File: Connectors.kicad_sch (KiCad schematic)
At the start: 16 parts, among them U2 LT3042IMSE

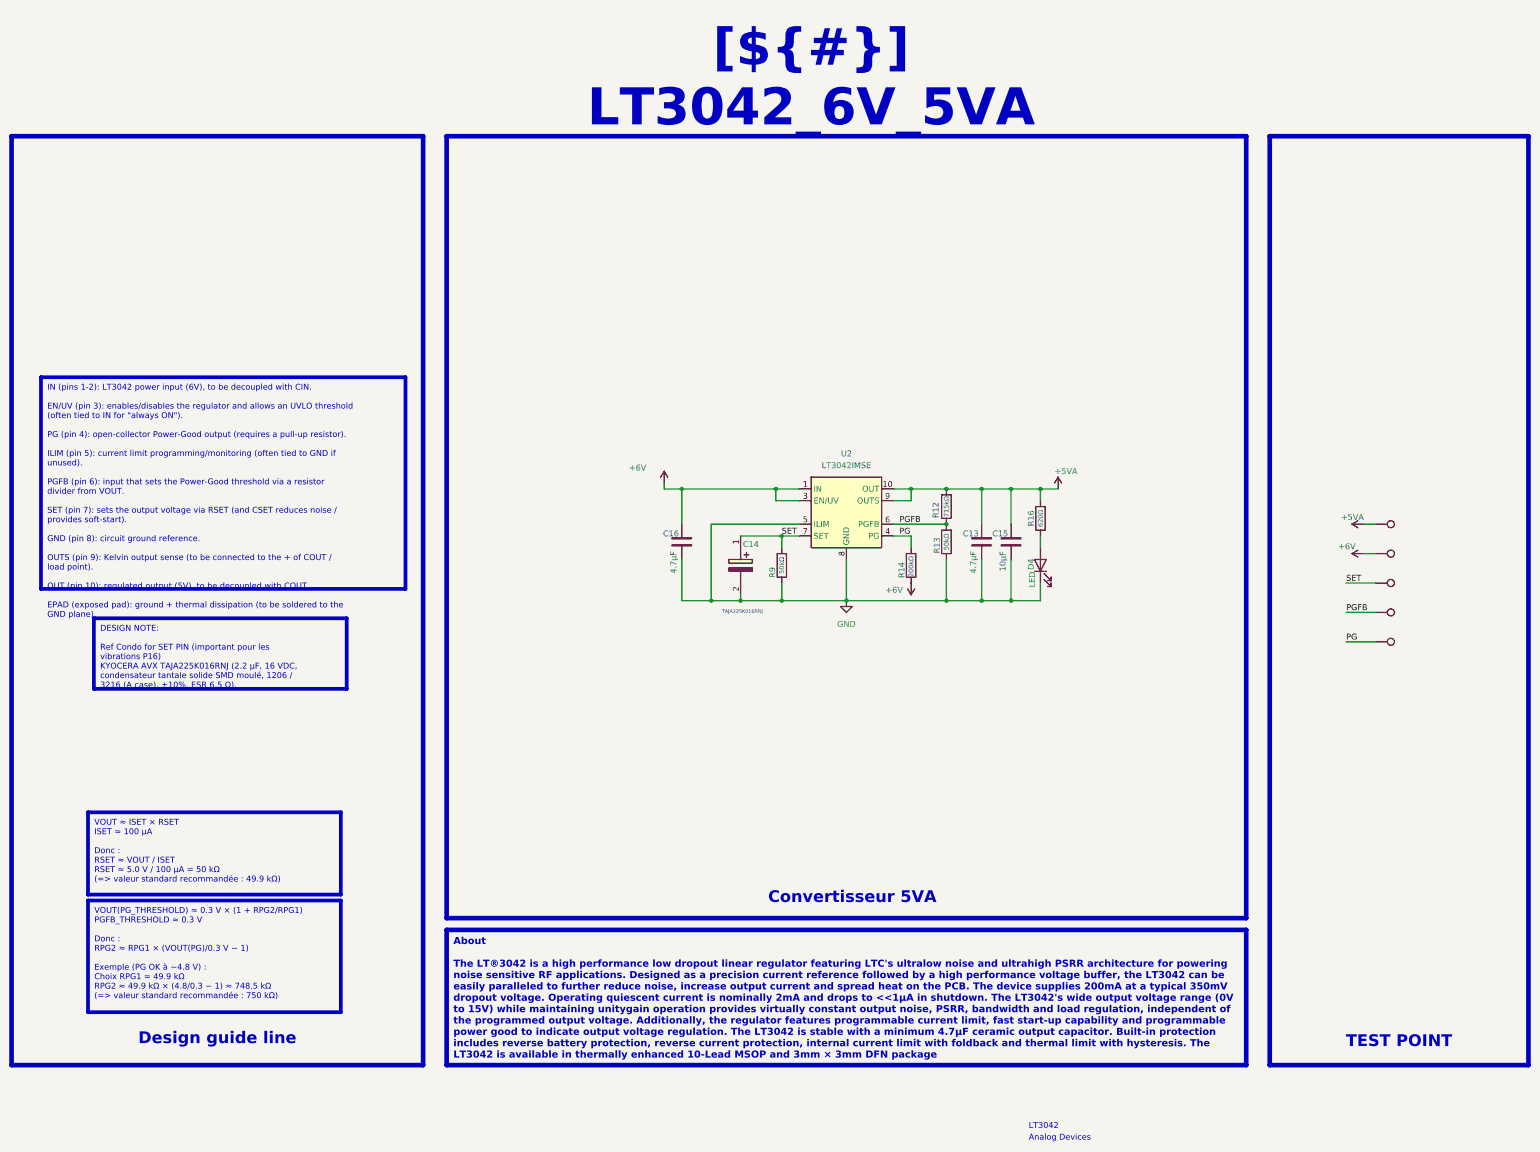
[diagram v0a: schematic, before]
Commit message: Clean up project for KDT template: rename, metadata, KiCad 10 CI
- Rename project Cellule_de_force_V2 -> OPEN_WEIGHT and sheets after their function
  (fix AD7910 -> AD7190 typo), update all sheet/project references in sch/pcb/pro
- Real title-block titles, sheet headers use ${TITLE}, restore KDT drawing sheets,
  remove template leftovers from PCB title block
- kibot_main.yaml: COMPANY = OPEN THRUST LAB, GIT_URL = foukouda/OPEN_WEIGHT
- CI: add KiCad 10 (KiBot v2_dk10), PRELIMINARY variant on dev
- README now generated from kibot_resources/templates/readme.txt; fill CHANGELOG
- Move mechanical CAD to Mechanical/, extend .gitignore, untrack 3Dx logs

Co-Authored-By: Claude Opus 5.5 <noreply@anthropic.com>
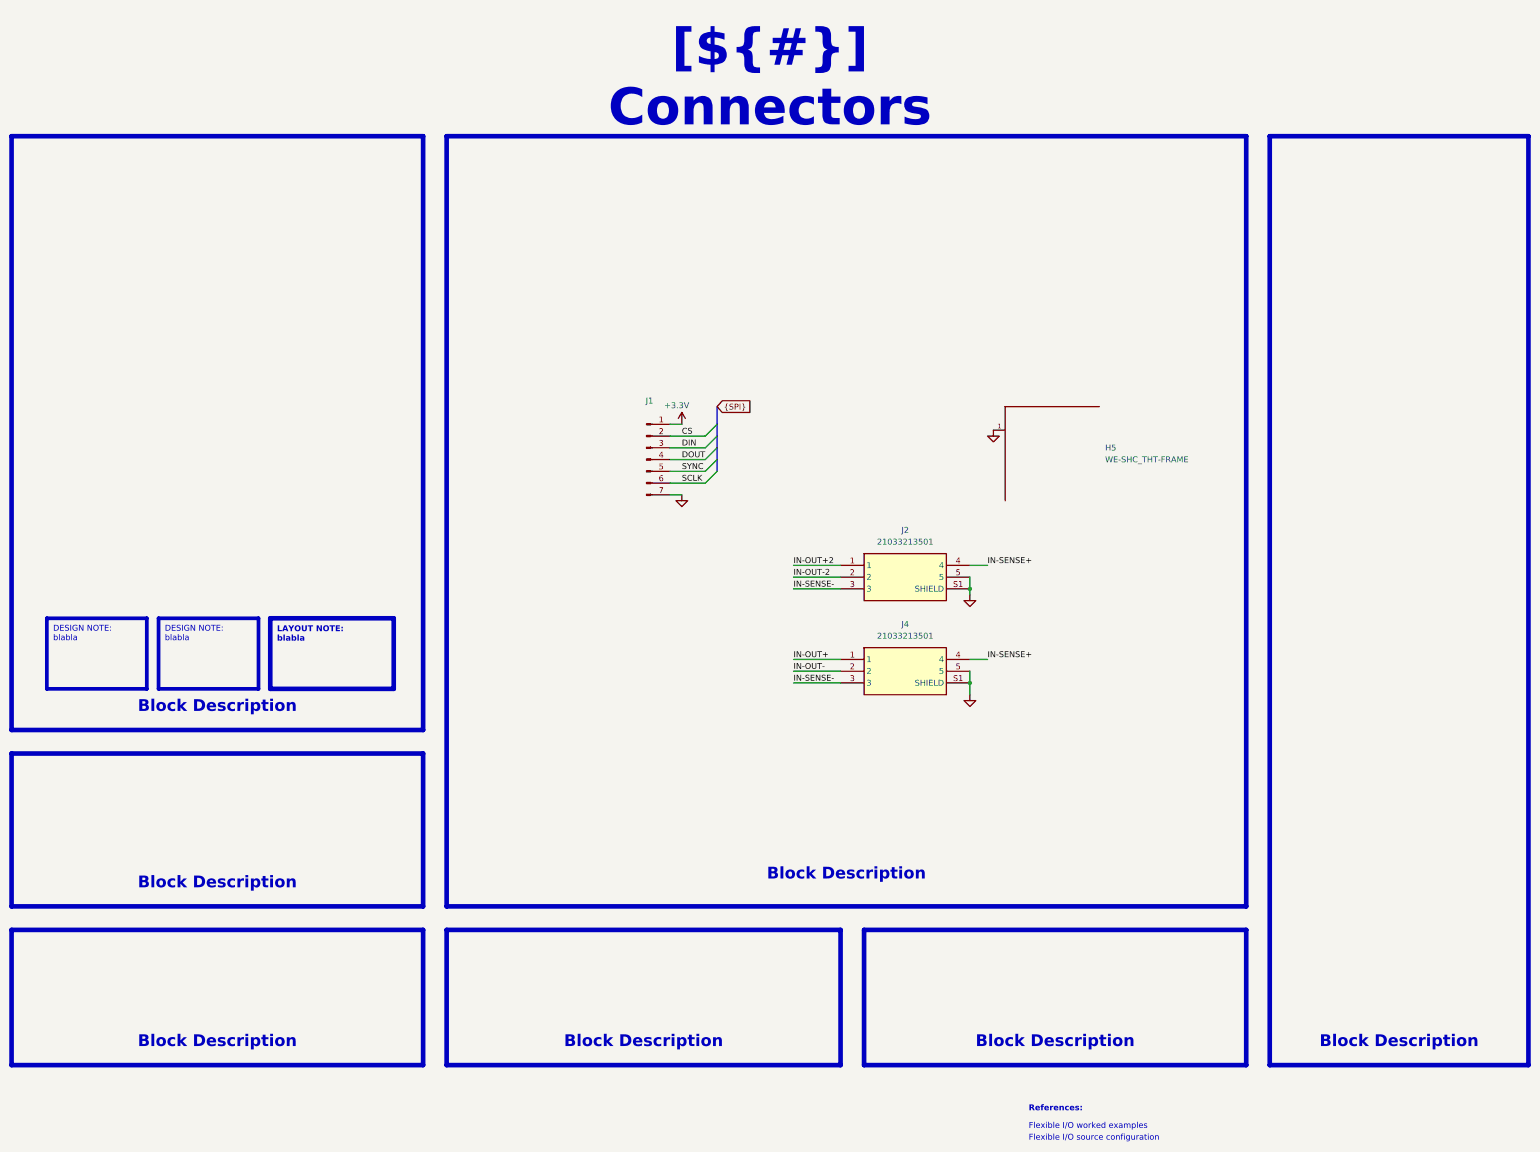
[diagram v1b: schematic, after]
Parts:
- removed C13, C16: 4.7µF, Capacitor_SMD:C_0603_1608Metric, symbol Device:C
- removed C14: TAJA225K016RNJ, CAPPM3216X180N, symbol TAJA225K016RNJ:TAJA225K016RNJ
- removed C15: 10µF, Capacitor_SMD:C_0603_1608Metric, symbol Device:C
- removed D4: LED, LED_SMD:LED_0603_1608Metric, symbol Device:LED
- removed R12: 715kΩ, Resistor_SMD:R_0603_1608Metric, symbol Device:R
- removed R13, R9: 50kΩ, Resistor_SMD:R_0603_1608Metric, symbol Device:R
- removed R14: 200kΩ, Resistor_SMD:R_0603_1608Metric, symbol Device:R
- removed R16: 620Ω, Resistor_SMD:R_0603_1608Metric, symbol Device:R
- removed TP10, TP11, TP12, TP13, TP17: TestPoint, TestPoint:TestPoint_Pad_D1.5mm, symbol Connector:TestPoint
- removed U2: LT3042IMSE, Package_SO:MSOP-10-1EP_3x3mm_P0.5mm_EP2.2x3.1mm_Mask1.83x1.89mm_ThermalVias, symbol Regulator_Linear:LT3042xMSE
- added H5: WE-SHC_THT-FRAME, WE-SHC_THT-FRAME:WE-SHC_THT-FRAME_36503205, symbol WE-SHC_THT-FRAME:WE-SHC_THT-FRAME
- added J1: Conn_01x07_Pin, Connector_JST:JST_XH_B7B-XH-AM_1x07_P2.50mm_Vertical, symbol Connector:Conn_01x07_Pin
- added J2, J4: 21033213501, 21033213501, symbol 21033213501:21033213501
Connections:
- net GND: now also H5.1, H5.10, H5.11, H5.12, H5.13, H5.14, H5.15, H5.16, H5.17, H5.2, H5.3, H5.4, H5.5, H5.6, H5.7, H5.9, J1.7 (Pin_7), J2.5, J2.S1 (SHIELD), J4.5, J4.S1 (SHIELD)
- new net +3.3V: J1.1 (Pin_1)
- new net CS: J1.2 (Pin_2)
- new net DIN: J1.3 (Pin_3)
- new net DOUT: J1.4 (Pin_4)
- new net IN-OUT+: J4.1
- new net IN-OUT+2: J2.1
- new net IN-OUT-: J4.2
- new net IN-OUT-2: J2.2
- new net IN-SENSE+: J2.4, J4.4
- new net IN-SENSE-: J2.3, J4.3
- new net SCLK: J1.6 (Pin_6)
- new net SYNC: J1.5 (Pin_5)
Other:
- note added: "Flexible I/O source configuration"
- note added: "Flexible I/O worked examples"
- note added: "References:"
- note removed: "Analog Devices"
- note removed: "LT3042"
- title: Sheet Title B -> Connectors

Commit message: Fix load-cell connectivity between Connectors and AD7190 sheets
IN-OUT/IN-SENSE were local labels on two sheets, so the connectors were not
connected to the ADC in the schematic. Convert them to global labels (IN-SENSE
merged into SENSE), and align label polarity on J2/J4 with the routed copper.

Co-Authored-By: Claude Opus 5.5 <noreply@anthropic.com>
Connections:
- net IN-SENSE+ renamed SENSE-
- net IN-SENSE- renamed SENSE+
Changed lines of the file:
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@@
 		)
 	)
-	(label "IN-SENSE+"
+	(global_label "SENSE-"
+		(shape bidirectional)
 		(at 256.54 152.4 0)
-		(effects
-			(font
-				(size 1.27 1.27)
-			)
-			(justify left bottom)
+		(fields_autoplaced yes)
+		(effects
+			(font
+				(size 1.27 1.27)
+			)
+			(justify left)
+		)
+		(property "Intersheetrefs" "${INTERSHEET_REFS}"
+			(at 266.5400 152.4 0)
+			(hide yes)
+			(show_name no)
+			(do_not_autoplace no)
+			(effects
+				(font
+					(size 1.27 1.27)
+				)
+				(justify left)
+			)
 		)
 	)
@@
 		)
 	)
-	(label "IN-SENSE+"
+	(global_label "SENSE-"
+		(shape bidirectional)
 		(at 256.54 132.08 0)
-		(effects
-			(font
-				(size 1.27 1.27)
-			)
-			(justify left bottom)
-		)
-	)
-	(label "IN-SENSE-"
+		(fields_autoplaced yes)
+		(effects
+			(font
+				(size 1.27 1.27)
+			)
+			(justify left)
+		)
+		(property "Intersheetrefs" "${INTERSHEET_REFS}"
+			(at 266.5400 132.08 0)
+			(hide yes)
+			(show_name no)
+			(do_not_autoplace no)
+			(effects
+				(font
+					(size 1.27 1.27)
+				)
+				(justify left)
+			)
+		)
+	)
+	(global_label "SENSE+"
+		(shape bidirectional)
 		(at 214.63 137.16 0)
-		(effects
-			(font
-				(size 1.27 1.27)
-			)
-			(justify left bottom)
+		(fields_autoplaced yes)
+		(effects
+			(font
+				(size 1.27 1.27)
+			)
+			(justify left)
+		)
+		(property "Intersheetrefs" "${INTERSHEET_REFS}"
+			(at 224.6300 137.16 0)
+			(hide yes)
+			(show_name no)
+			(do_not_autoplace no)
+			(effects
+				(font
+					(size 1.27 1.27)
+				)
+				(justify left)
+			)
 		)
 	)
@@
 		)
 	)
-	(label "IN-SENSE-"
+	(global_label "SENSE+"
+		(shape bidirectional)
 		(at 214.63 157.48 0)
-		(effects
-			(font
-				(size 1.27 1.27)
-			)
-			(justify left bottom)
+		(fields_autoplaced yes)
+		(effects
+			(font
+				(size 1.27 1.27)
+			)
+			(justify left)
+		)
+		(property "Intersheetrefs" "${INTERSHEET_REFS}"
+			(at 224.6300 157.48 0)
+			(hide yes)
+			(show_name no)
+			(do_not_autoplace no)
+			(effects
+				(font
+					(size 1.27 1.27)
+				)
+				(justify left)
+			)
 		)
 	)
@@
 		)
 	)
-	(label "IN-OUT+2"
+	(global_label "IN-OUT+2"
+		(shape bidirectional)
 		(at 214.63 132.08 0)
-		(effects
-			(font
-				(size 1.27 1.27)
-			)
-			(justify left bottom)
+		(fields_autoplaced yes)
+		(effects
+			(font
+				(size 1.27 1.27)
+			)
+			(justify left)
+		)
+		(property "Intersheetrefs" "${INTERSHEET_REFS}"
+			(at 224.6300 132.08 0)
+			(hide yes)
+			(show_name no)
+			(do_not_autoplace no)
+			(effects
+				(font
+					(size 1.27 1.27)
+				)
+				(justify left)
+			)
 		)
 	)
@@
 		)
 	)
-	(label "IN-OUT+"
+	(global_label "IN-OUT+"
+		(shape bidirectional)
 		(at 214.63 152.4 0)
-		(effects
-			(font
-				(size 1.27 1.27)
-			)
-			(justify left bottom)
-		)
-	)
-	(label "IN-OUT-2"
+		(fields_autoplaced yes)
+		(effects
+			(font
+				(size 1.27 1.27)
+			)
+			(justify left)
+		)
+		(property "Intersheetrefs" "${INTERSHEET_REFS}"
+			(at 224.6300 152.4 0)
+			(hide yes)
+			(show_name no)
+			(do_not_autoplace no)
+			(effects
+				(font
+					(size 1.27 1.27)
+				)
+				(justify left)
+			)
+		)
+	)
+	(global_label "IN-OUT-2"
+		(shape bidirectional)
 		(at 214.63 134.62 0)
-		(effects
-			(font
-				(size 1.27 1.27)
-			)
-			(justify left bottom)
-		)
-	)
-	(label "IN-OUT-"
+		(fields_autoplaced yes)
+		(effects
+			(font
+				(size 1.27 1.27)
+			)
+			(justify left)
+		)
+		(property "Intersheetrefs" "${INTERSHEET_REFS}"
+			(at 224.6300 134.62 0)
+			(hide yes)
+			(show_name no)
+			(do_not_autoplace no)
+			(effects
+				(font
+					(size 1.27 1.27)
+				)
+				(justify left)
+			)
+		)
+	)
+	(global_label "IN-OUT-"
+		(shape bidirectional)
 		(at 214.63 154.94 0)
-		(effects
-			(font
-				(size 1.27 1.27)
-			)
-			(justify left bottom)
-		)
-	)
+		(fields_autoplaced yes)
+		(effects
+			(font
+				(size 1.27 1.27)
+			)
+			(justify left)
+		)
+		(property "Intersheetrefs" "${INTERSHEET_REFS}"
+			(at 224.6300 154.94 0)
+			(hide yes)
+			(show_name no)
+			(do_not_autoplace no)
+			(effects
+				(font
+					(size 1.27 1.27)
+				)
+				(justify left)
+			)
+		)
+	)

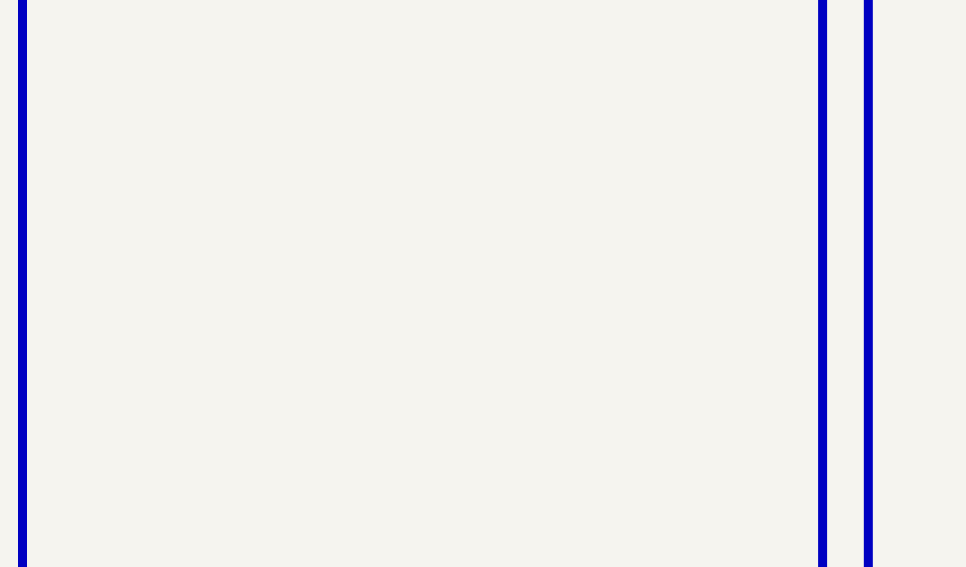
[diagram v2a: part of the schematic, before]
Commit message: Self-contained libraries, JLCPCB rules, ERC/DRC cleanup
- lib/: project symbol library (19 symbols), footprint library (17 footprints)
  and all 3D models (15), referenced through ${KIPRJMOD} + project lib tables.
  A fresh clone now opens with every symbol, footprint and 3D model.
- Remove duplicated / absolute 3D model paths (C:/Users/..., ${KICAD_FOOTPRINT})
- OPEN_WEIGHT.kicad_dru: JLCPCB 4-layer rules; stackup JLC04161H-7628; board minimums
- AD7190 footprint: drop per-pad 0.102 mm mask margin (mask bridges at 0.65 mm pitch)
- Exclude unplaced TP/FID symbols from board; PWR_FLAGs; decorative wires -> lines
- Local text variables in .kicad_pro; Revision History wired to [Unreleased]
- get_changelog.py: accept "## [Unreleased]" without date
ERC: 0 errors. DRC: 0 errors except 10 courtyard overlaps (placement), 0 parity issues.

Co-Authored-By: Claude Opus 5.5 <noreply@anthropic.com>
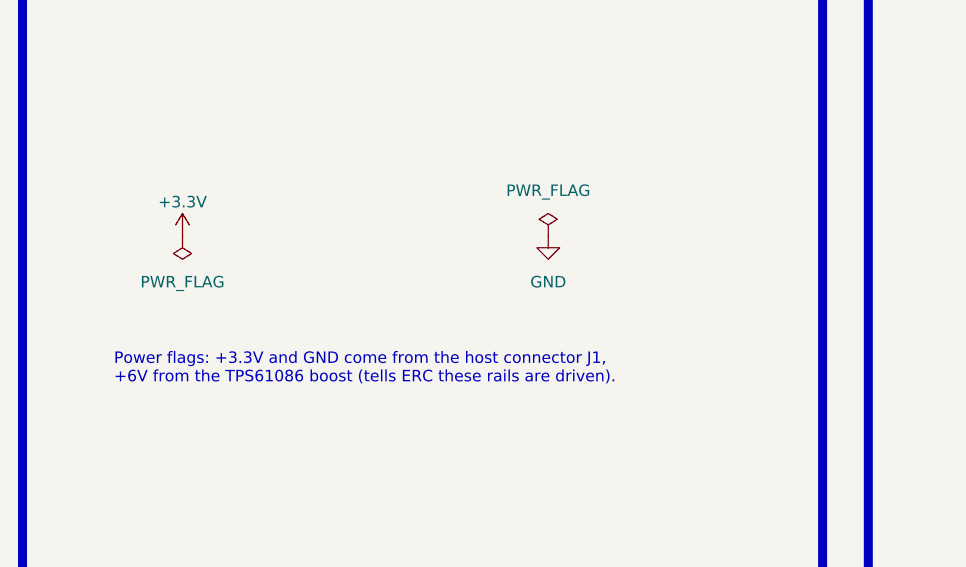
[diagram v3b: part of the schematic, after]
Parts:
- H5: footprint WE-SHC_THT-FRAME:WE-SHC_THT-FRAME_36503205 -> OPEN_WEIGHT:WE-SHC_THT-FRAME_36503205; symbol WE-SHC_THT-FRAME:WE-SHC_THT-FRAME -> OPEN_WEIGHT:WE-SHC_THT-FRAME
- J1: footprint Connector_JST:JST_XH_B7B-XH-AM_1x07_P2.50mm_Vertical -> OPEN_WEIGHT:JST_XH_B7B-XH-AM_1x07_P2.50mm_Vertical; symbol Connector:Conn_01x07_Pin -> OPEN_WEIGHT:Conn_01x07_Pin
- J2, J4: footprint 21033213501 -> OPEN_WEIGHT:21033213501; symbol 21033213501:21033213501 -> OPEN_WEIGHT:21033213501
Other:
- note added: "Power flags: +3.3V and GND come from the host connector J1, +6V from the TPS61086 boost (tells ERC these rails are driven)."
